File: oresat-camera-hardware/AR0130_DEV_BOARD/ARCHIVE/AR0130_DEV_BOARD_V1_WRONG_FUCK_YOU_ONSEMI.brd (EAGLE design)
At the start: 40 x 44 mm, 86 parts, among them J2 4-1734592-04-1734592-0, U10 SN74AVCB164245VR, U11 KC2520B27.0000C10E00, U12 TPS71818-33DRVT, U13 SN74AVCH8T245RHLR, U14 TPS71928-28DRVT, U15 TPS71928-28DRVT, U6 MCP9808T-E/MCDFN8_2X3MC-M, U7 MCP9808T-E/MCDFN8_2X3MC-M, U9 TCA9509DGKRDGK8-M

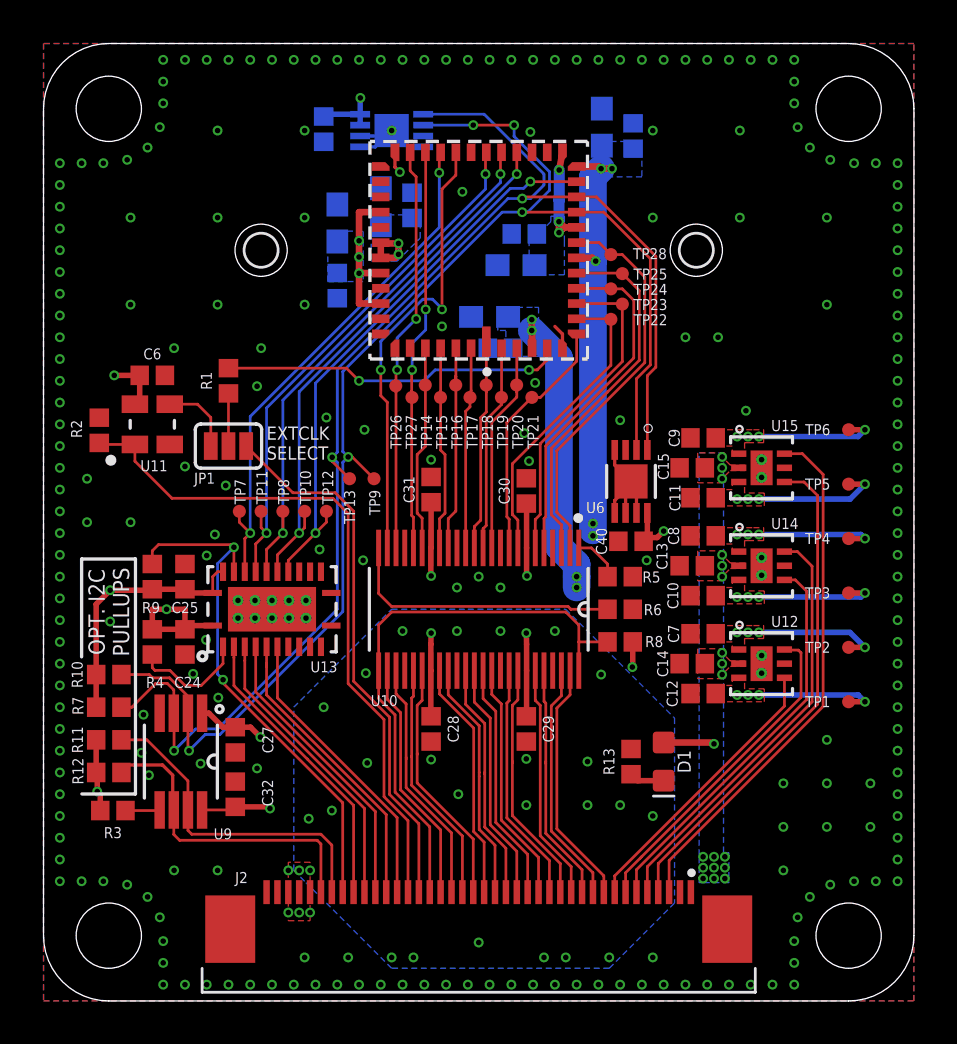
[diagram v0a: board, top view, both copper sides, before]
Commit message: EVERYTHING IS FINE. Updated board for totally correct footprint this time I swear
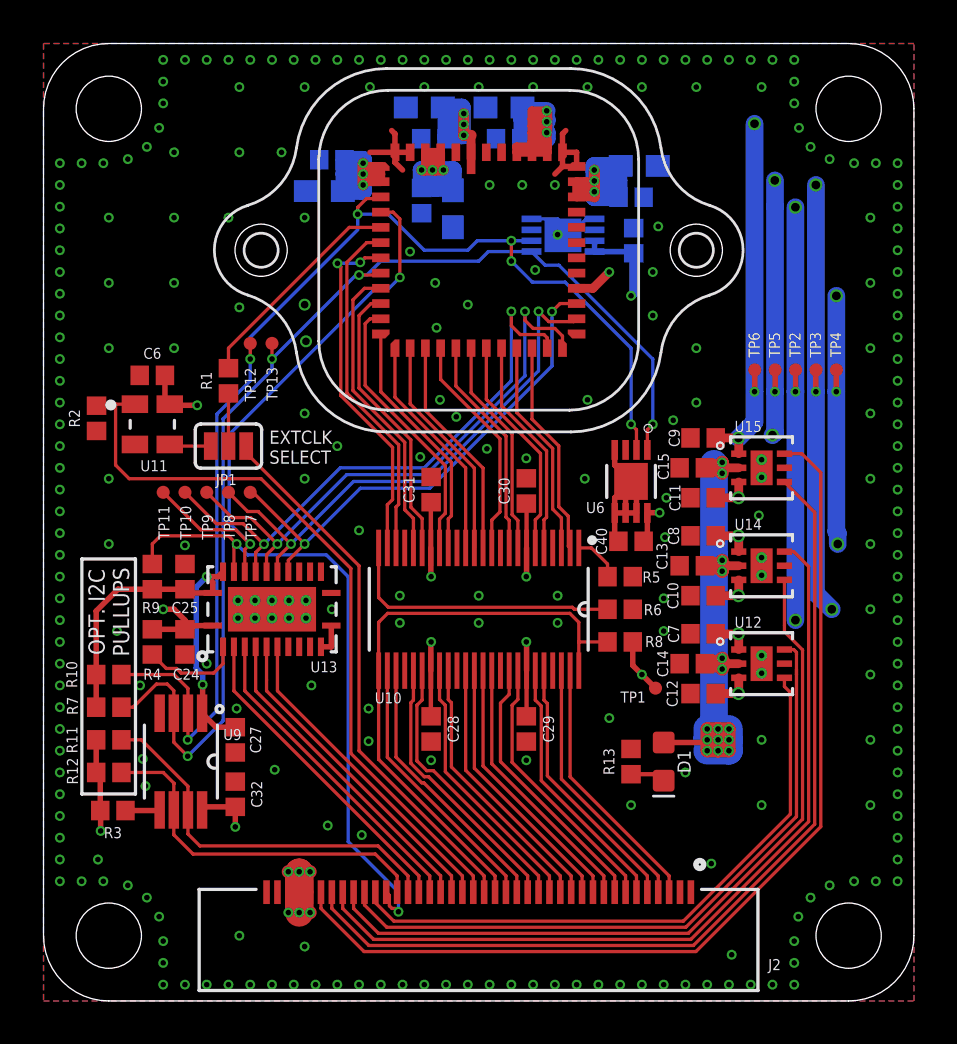
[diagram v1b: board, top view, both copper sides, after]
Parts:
- removed TP14, TP15, TP16, TP17, TP18, TP19, TP20, TP21, TP22, TP23, TP24, TP25, TP26, TP27, TP28: TPTP06R, testpad:TP06R
- removed U$3: (no value), Oliver_Custom:PSAS_LOGO_15X15
- J2: value 4-1734592-04-1734592-0 -> 4-1734592-0; device Oliver_Custom:TE_4-1734592-0 -> Oliver_Custom:CONN_4-1734592-0_TYCO
- U$2: value AR0130CSSM00SPCA0−DRBR1-847AC-ILCC -> AR0130CSSM00SPCA0−DRBR1-847AB
- moved C39 15.1 mm to (27.1, 34.9), turned to 90 degrees
- moved C20 13.9 mm to (13.2, 38.7), turned to 0 degrees
- moved C2 13.1 mm to (12.9, 37.2), turned to 0 degrees
- moved TP2 13.0 mm to (34.6, 29.0)
- moved C5 12.0 mm to (27.4, 38.4), turned to 180 degrees
- moved C21 10.4 mm to (21.4, 39.6), turned to 0 degrees
- moved TP3 10.4 mm to (35.5, 29.0)
- moved C22 10.1 mm to (17.9, 39.6)
- moved C4 10.1 mm to (17.5, 41.1)
- moved C23 10.1 mm to (27.0, 36.9), turned to 180 degrees
- moved C3 9.32 mm to (21.2, 41.1), turned to 0 degrees
- moved U7 9.23 mm to (23.9, 35.2), turned to 180 degrees
- moved TP1 8.90 mm to (28.1, 14.4)
- moved TP12 8.43 mm to (9.50, 30.2)
- moved TP4 7.77 mm to (36.4, 29.0)
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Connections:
- net 1.8V: now also U$2.3, U$2.34, U$2.4; no longer U$2.14, U$2.19
- net 2.8V: now also U$2.7, U$2.8; no longer U$2.12, U$2.18
- net 3.3V_EN: now also J2.30; no longer J2.8
- net CLK_EN: now also J2.21; no longer J2.27
- net DE_0: now also J2.3, U10.47; no longer J2.21, U10.30
- net DE_1: now also J2.4, U10.46; no longer J2.20, U10.32
- net DE_10: now also J2.13, U10.33; no longer J2.11, U10.44
- net DE_11: now also J2.14, U10.32; no longer J2.10, U10.46
- net DE_2: now also J2.5, U10.44; no longer J2.19, U10.33
- net DE_3: now also J2.6, U10.43; no longer J2.18, U10.35
- net DE_4: now also J2.7, U10.41; no longer J2.17, U10.36
- net DE_5: now also J2.8, U10.40; no longer J2.16, U10.37
- net DE_6: now also J2.9; no longer J2.15
- net DE_7: now also J2.10, U10.37; no longer J2.14, U10.40
- net DE_8: now also J2.11, U10.36; no longer J2.13, U10.41
- net DE_9: now also U10.35; no longer U10.43
- net DI_0: now also U$2.28, U10.2; no longer TP14.TP, U$2.45, U10.19
- net DI_1: now also U$2.27, U10.3; no longer TP15.TP, U$2.46, U10.17
- net DI_10: now also U$2.18, U10.16; no longer TP24.TP, U$2.10, U10.5
- net DI_11: now also U$2.17, U10.17; no longer TP25.TP, U$2.11, U10.3
- net DI_2: now also U$2.26, U10.5; no longer TP16.TP, U$2.47, U10.16
- net DI_3: now also U$2.25, U10.6; no longer TP17.TP, U$2.48, U10.14
- net DI_4: now also U$2.24, U10.8; no longer TP18.TP, U$2.1, U10.13
- net DI_5: now also U$2.23, U10.9; no longer TP19.TP, U$2.2, U10.12
- net DI_6: now also U$2.22; no longer TP20.TP, U$2.3
- net DI_7: now also U$2.21, U10.12; no longer TP21.TP, U$2.7, U10.9
- net DI_8: now also U$2.20, U10.13; no longer TP22.TP, U$2.8, U10.8
- net DI_9: now also U$2.19, U10.14; no longer TP23.TP, U$2.9, U10.6
- net EXTCLK_E: now also J2.20; no longer J2.26
- net FLASH_E: now also J2.18; no longer J2.24
- net FLASH_I: now also U$2.13; no longer U$2.26
- net GND: now also U$2.2, U$2.38, U$2.42, U$2.43, U$2.47, U$2.48, U$2.5; no longer J2.S1, J2.S2, U$2.25, U$2.30, U$2.35, U$2.44
- net HSYNC_E: now also J2.15, U10.30; no longer J2.23, U10.27
- net HSYNC_I: now also U$2.16, U10.19; no longer TP26.TP, U$2.29, U10.22
- net INPUT_DRVR_EN: now also J2.29; no longer J2.33
- net N$1: now also U$2.11; no longer U$2.5
- net OE_BAR_E: now also J2.23, U13.6; no longer J2.30, U13.5
- net OE_BAR_I: now also U$2.32, U13.18; no longer U$2.23, U13.19
- net OUTPUT_DRVR_EN: now also J2.19; no longer J2.25
- net PIXCLK_E: now also J2.17, U10.27; no longer J2.9, U10.47
- net PIXCLK_I: now also U$2.12, U10.22; no longer TP28.TP, U$2.13, U10.2
- net RST_BAR_E: now also J2.24, U13.5; no longer J2.28, U13.7
- net RST_BAR_I: now also U$2.30, U13.19; no longer U$2.17, U13.17
- net SADDR_E: now also J2.26, U13.3; no longer J2.31, U13.4
- net SADDR_I: now also U$2.10, U13.21; no longer U$2.24, U13.20
- net SCL_E: now also J2.27; no longer J2.34
- net SCL_I: now also U$2.9; no longer U$2.15
- net SDA_E: now also J2.28; no longer J2.35
- net SDA_I: now also U$2.14; no longer U$2.16
- net STANDBY_E: now also J2.25, U13.4; no longer J2.29, U13.6
- net STANDBY_I: now also U$2.29, U13.20; no longer U$2.22, U13.18
- net TRIG_E: now also J2.22, U13.7; no longer J2.32, U13.3
- net TRIG_I: now also U$2.33, U13.17; no longer U$2.27, U13.21
- net VAA_EN: now also J2.35; no longer J2.3
- net VAA_PIX_EN: now also J2.34; no longer J2.4
- net VCC: now also U$2.44, U$2.45, U$2.46; no longer U$2.34, U$2.38, U$2.40
- net VCC_1: now also U$2.1; no longer U$2.4
- net VCC_2: now also U$2.40, U$2.41; no longer U$2.36, U$2.37
- net VDD18_EN: now also J2.31; no longer J2.7
- net VDD_IO_EN: now also J2.33; no longer J2.5
- net VDD_PLL_EN: now also J2.32; no longer J2.6
- net VSYNC_E: now also J2.16; no longer J2.22
- net VSYNC_I: now also U$2.15; no longer TP27.TP, U$2.28
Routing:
- net 5V: track 2.38 -> 70.4 mm, vias 25 -> 21
- net VCC_1: track 28.9 -> 52.9 mm, vias 8 -> 7
- net VAA_EN: track 24.3 -> 45.2 mm
- net VAA_PIX_EN: track 23.0 -> 42.3 mm
- net VDD_IO_EN: track 19.7 -> 38.1 mm
- net VDD_PLL_EN: track 18.3 -> 35.4 mm
- net 1.8V: track 41.3 -> 58.2 mm, vias 7 -> 8
- net VDD18_EN: track 15.2 -> 31.5 mm
- net 3.3V_EN: track 13.1 -> 28.3 mm
- net 3.3V: track 80.9 -> 68.8 mm, vias 10 -> 7
- net SDA_I: track 65.1 -> 53.8 mm, vias 3 -> 4
- net GND: track 13.3 -> 24.4 mm, vias 247 -> 255
- net VCC: track 35.9 -> 44.9 mm, vias 7 -> 6
- net SCL_I: track 65.3 -> 57.1 mm, vias 5 -> 6
- net HSYNC_I: track 19.0 -> 13.1 mm, vias 2 -> 0
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- removed copper zone on layer 1, net 1.8V
- removed copper zone on layer 16, net 1.8V
- removed copper zone on layer 1, net 2.8V
- removed copper zone on layer 16, net 2.8V
- removed copper zone on layer 1, net 3.3V
- removed copper zone on layer 1, net 5V
- removed copper zone on layer 15, net 5V
- removed copper zone on layer 16, net 5V
- removed copper zone on layer 1, net VCC
- removed copper zone on layer 16, net VCC
- removed copper zone on layer 1, net VCC_1
- removed copper zone on layer 16, net VCC_1
- removed copper zone on layer 1, net VCC_2
- removed copper zone on layer 16, net VCC_2
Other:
- board text added: "AR0130-DEV-BOARD ORESAT 2018-04-06 OLIVER REW"
- board text removed: "AR0130-DEV-BOARD REV.2 ORESAT 2018-05-28 OLIVER REW"
